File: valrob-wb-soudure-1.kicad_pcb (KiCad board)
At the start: 2 copper layers, 31 parts, among them J1 Conn_01x03, J2 Conn_01x06, J3 Conn_01x02, J4 Conn_01x02, J5 Conn_01x02, J6 Conn_01x02, Q1 2N7000, SW1 SW_Push, SW2 SW_Push, SW3 SW_Push, SW4 SW_Push

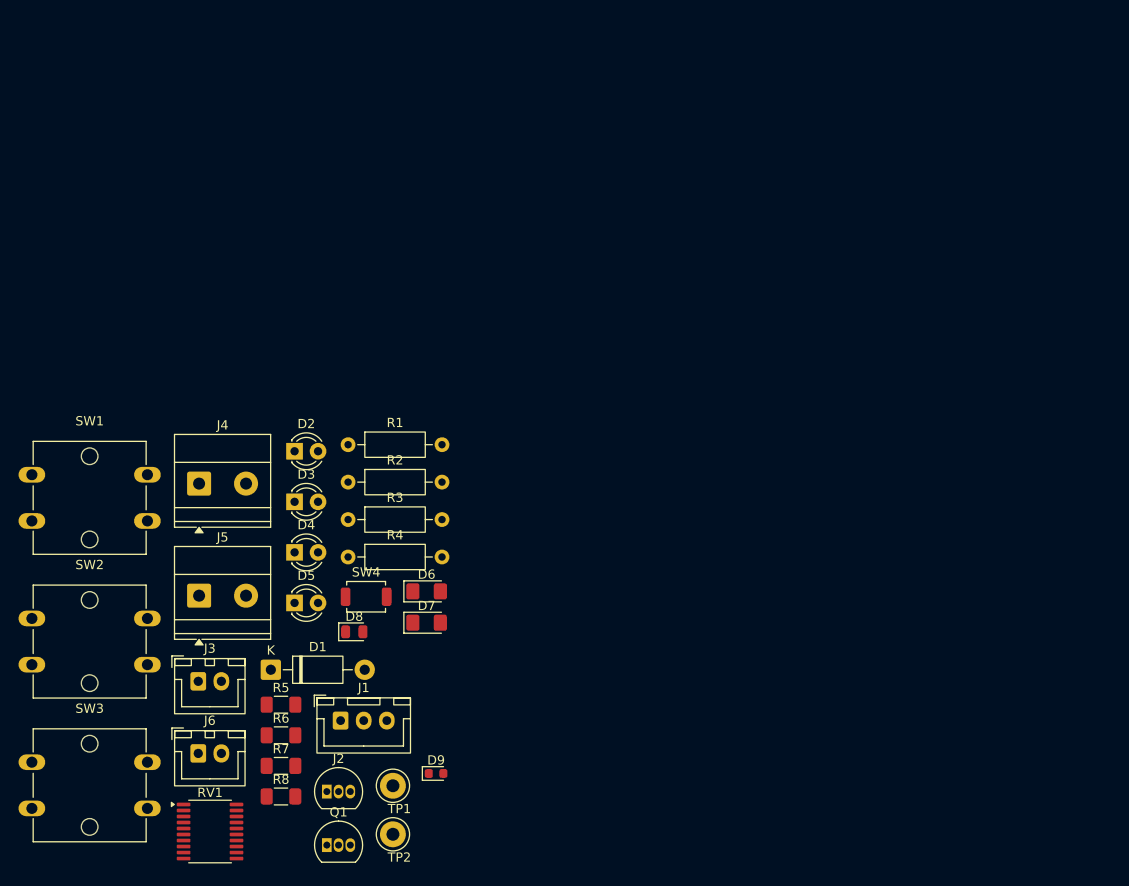
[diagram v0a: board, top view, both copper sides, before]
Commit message: pcb: initial sectionning
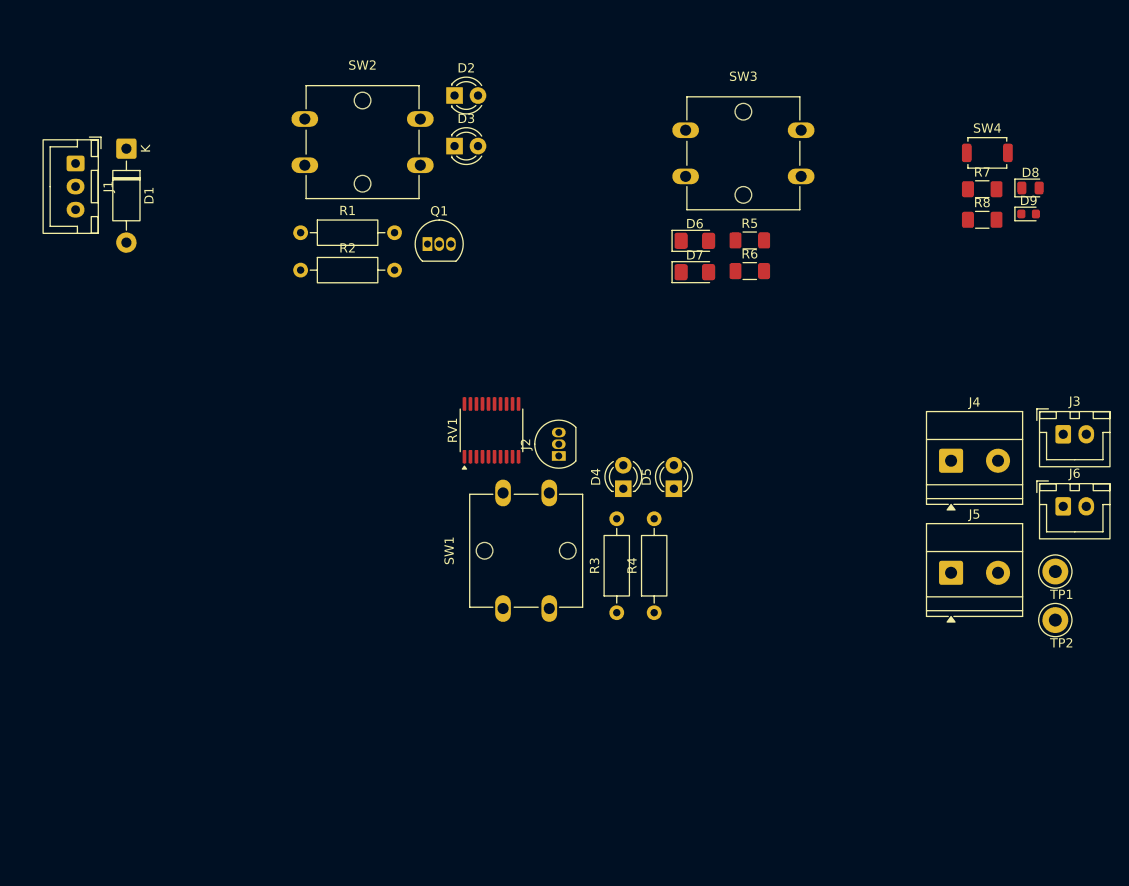
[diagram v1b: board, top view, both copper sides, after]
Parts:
- moved SW3 98.4 mm to (118.8, 103.2)
- moved R7 98.2 mm to (150.8, 109.6)
- moved R8 98.2 mm to (150.8, 112.9)
- moved J3 97.3 mm to (159.6, 136.2)
- moved J6 97.3 mm to (159.6, 143.9)
- moved D9 88.2 mm to (155.9, 112.3)
- moved D8 87.5 mm to (156.1, 109.5)
- moved SW4 82.6 mm to (151.4, 105.7)
- moved J4 81.4 mm to (147.5, 139.0)
- moved J5 81.4 mm to (147.5, 151.1)
- moved TP1 75.3 mm to (158.8, 151.0)
- moved TP2 75.3 mm to (158.8, 156.2)
- moved R6 71.4 mm to (125.7, 118.5)
- moved R5 71.4 mm to (125.7, 115.2)
- moved J1 66.7 mm to (52.8, 106.8), turned to -90 degrees
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
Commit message: pcb: add pot 3d model
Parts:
- RV1: footprint Package_SO:TSSOP-20_4.4x6.5mm_P0.65mm -> Potentiometer_THT:Potentiometer_Alps_RK09Y11_Single_Horizontal
- moved R2 25.5 mm to (87.0, 94.9), turned to -90 degrees
- moved D2 24.5 mm to (79.0, 119.0), turned to 90 degrees
- moved SW3 21.4 mm to (98.0, 98.0)
- moved D3 15.6 mm to (87.0, 119.0), turned to 90 degrees
- moved SW2 10.4 mm to (68.0, 98.0)
- moved R1 8.51 mm to (68.9, 112.0)
- moved D1 6.97 mm to (60.0, 112.0), turned to 90 degrees
- moved Q1 6.22 mm to (85.7, 112.0)
- moved RV1 5.90 mm to (95.0, 130.5), turned to 0 degrees
- moved J1 2.95 mm to (52.0, 104.0)

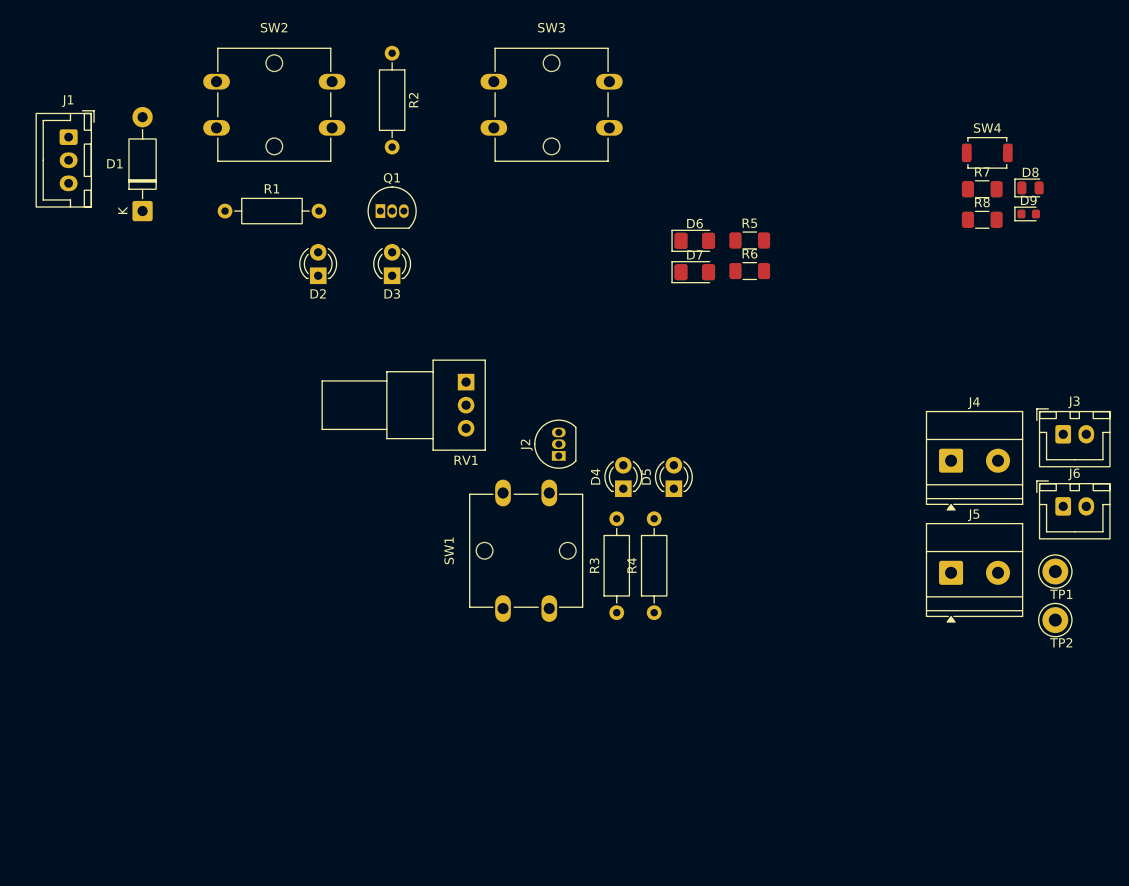
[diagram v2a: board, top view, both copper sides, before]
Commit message: pcb: initial layout
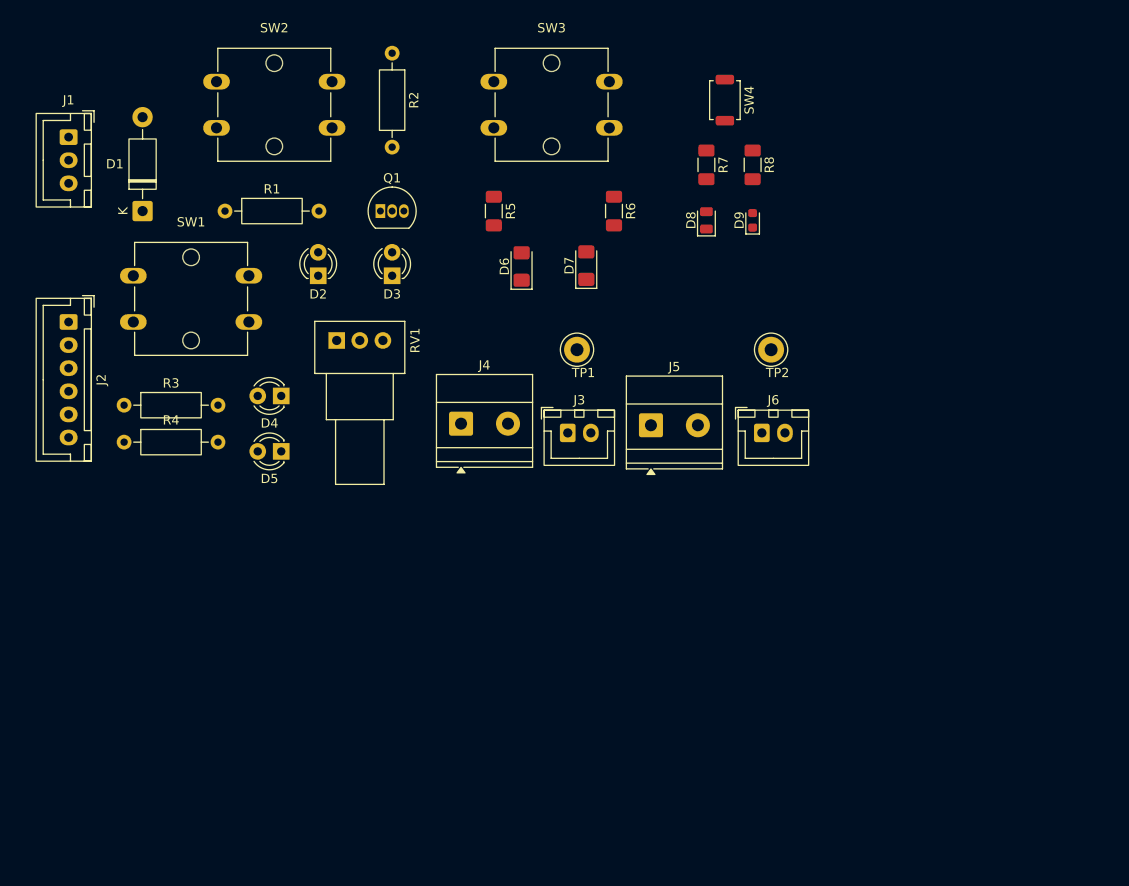
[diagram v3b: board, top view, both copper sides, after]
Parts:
- J2: footprint Package_TO_SOT_THT:TO-92_Inline -> Connector_JST:JST_XH_B6B-XH-A_1x06_P2.50mm_Vertical
- moved R4 60.2 mm to (58.0, 137.0), turned to 0 degrees
- moved R3 57.8 mm to (58.0, 133.0), turned to 0 degrees
- moved TP1 57.0 mm to (107.0, 127.0)
- moved J2 55.0 mm to (52.0, 124.0), turned to -90 degrees
- moved SW1 53.8 mm to (59.0, 119.0), turned to 0 degrees
- moved J3 53.6 mm to (106.0, 136.0)
- moved J4 53.2 mm to (94.5, 135.0)
- moved D5 42.7 mm to (75.0, 138.0), turned to 180 degrees
- moved TP2 42.4 mm to (128.0, 127.0)
- moved D4 38.3 mm to (75.0, 132.0), turned to 180 degrees
- moved J5 36.2 mm to (115.0, 135.2)
- moved D8 35.2 mm to (121.0, 113.0), turned to 90 degrees
- moved J6 33.6 mm to (127.0, 136.0)
- moved R7 30.0 mm to (121.0, 107.0), turned to -90 degrees
- moved D9 29.9 mm to (126.0, 113.0), turned to 90 degrees
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
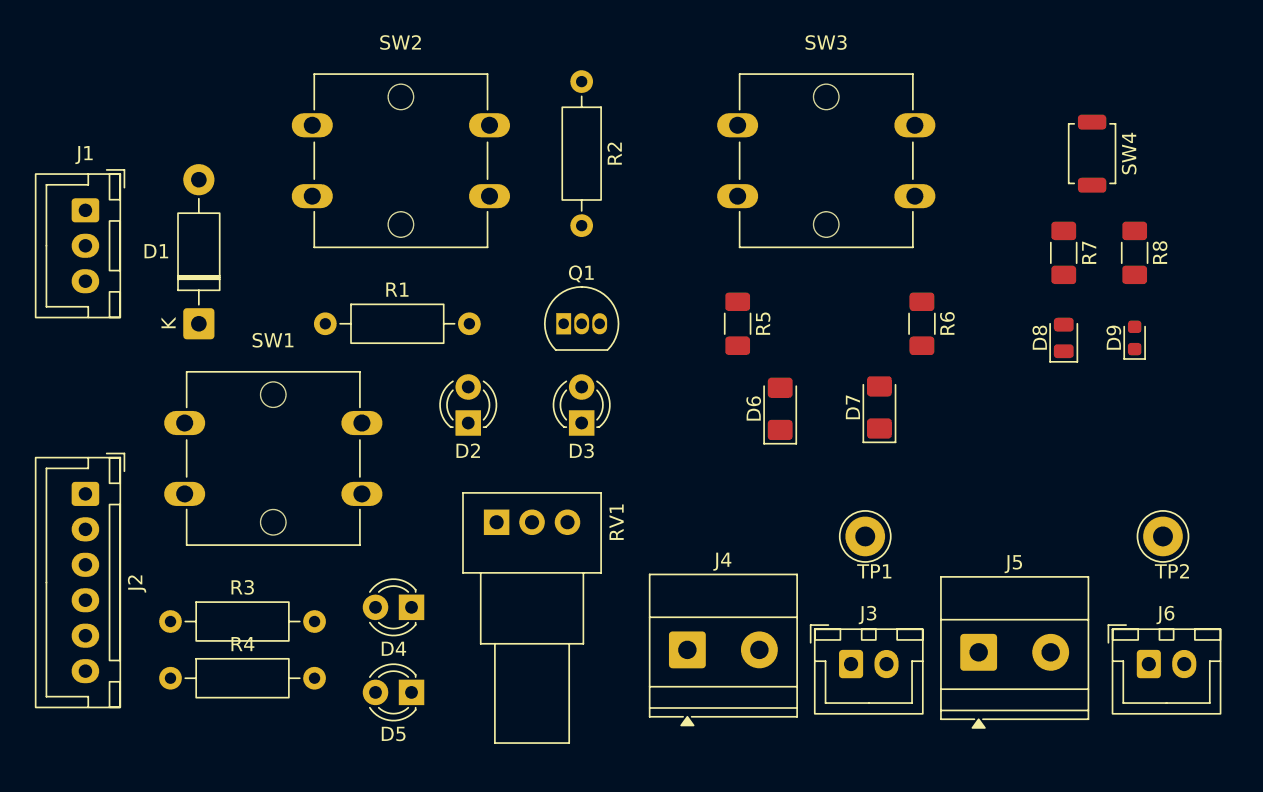
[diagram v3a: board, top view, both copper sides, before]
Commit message: pcb: add edge cut
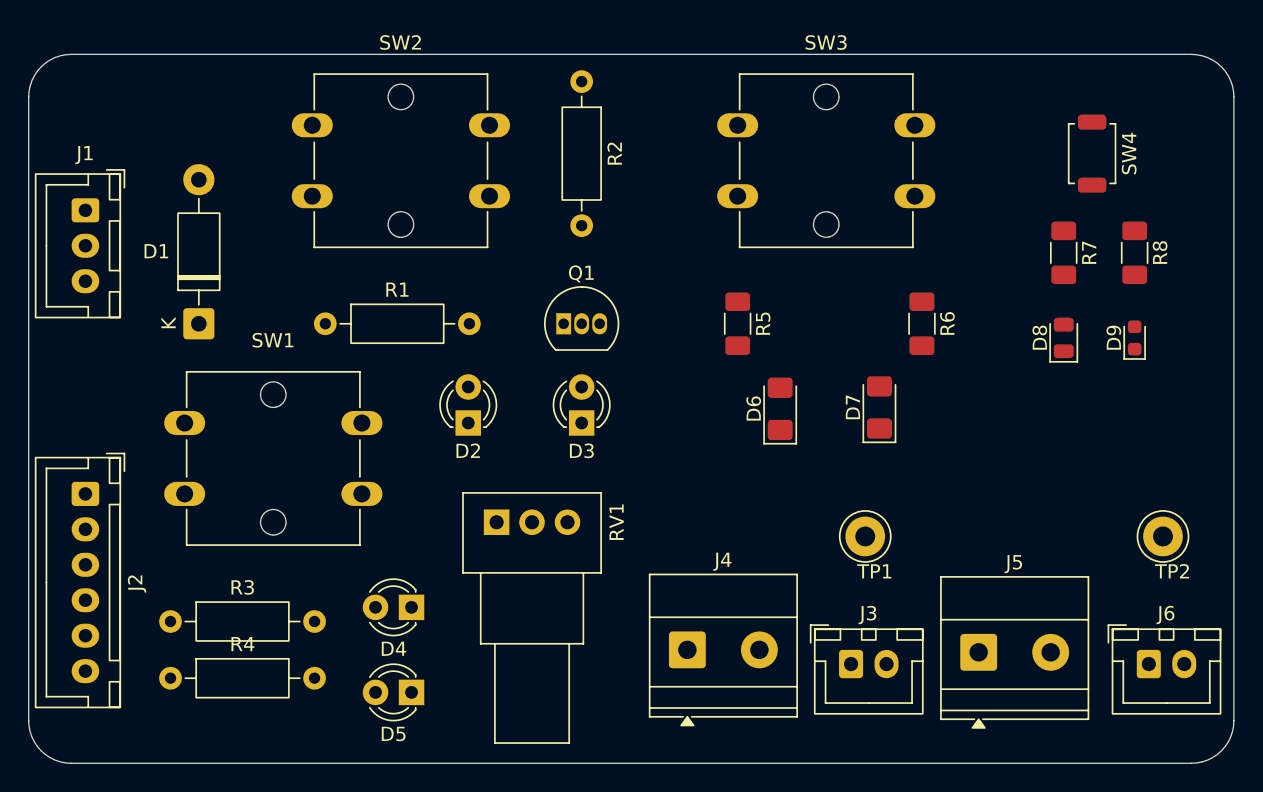
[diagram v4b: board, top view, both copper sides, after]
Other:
- board outline added: 85 x 50 mm
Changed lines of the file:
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@@
 		)
+	)
+	(gr_arc
+		(start 48 96)
+		(mid 48.87868 93.87868)
+		(end 51 93)
+		(stroke
+			(width 0.05)
+			(type default)
+		)
+		(layer "Edge.Cuts")
+	)
+	(gr_line
+		(start 48 140)
+		(end 48 96)
+		(stroke
+			(width 0.05)
+			(type default)
+		)
+		(layer "Edge.Cuts")
+	)
+	(gr_line
+		(start 51 93)
+		(end 130 93)
+		(stroke
+			(width 0.05)
+			(type default)
+		)
+		(layer "Edge.Cuts")
+	)
+	(gr_arc
+		(start 51 143)
+		(mid 48.87868 142.12132)
+		(end 48 140)
+		(stroke
+			(width 0.05)
+			(type default)
+		)
+		(layer "Edge.Cuts")
+	)
+	(gr_arc
+		(start 130 93)
+		(mid 132.12132 93.87868)
+		(end 133 96)
+		(stroke
+			(width 0.05)
+			(type default)
+		)
+		(layer "Edge.Cuts")
+	)
+	(gr_line
+		(start 130 143)
+		(end 51 143)
+		(stroke
+			(width 0.05)
+			(type default)
+		)
+		(layer "Edge.Cuts")
+	)
+	(gr_line
+		(start 133 96)
+		(end 133 140)
+		(stroke
+			(width 0.05)
+			(type default)
+		)
+		(layer "Edge.Cuts")
+	)
+	(gr_arc
+		(start 133 140)
+		(mid 132.12132 142.12132)
+		(end 130 143)
+		(stroke
+			(width 0.05)
+			(type default)
+		)
+		(layer "Edge.Cuts")
 	)
 	(embedded_fonts no)

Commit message: schem/pcb: add M3 mouting holes
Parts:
- added H1: MountingHole_Pad, MountingHole:MountingHole_3.2mm_M3_Pad_Via, F.Cu at (128.0, 98.0)
- added H2: MountingHole_Pad, MountingHole:MountingHole_3.2mm_M3_Pad_Via, F.Cu at (53.0, 98.0)
- added H3: MountingHole_Pad, MountingHole:MountingHole_3.2mm_M3_Pad_Via, F.Cu at (128.0, 138.0)
- added H4: MountingHole_Pad, MountingHole:MountingHole_3.2mm_M3_Pad_Via, F.Cu at (53.0, 138.0)
- moved J6 15.6 mm to (117.0, 124.0)
- moved J2 6.00 mm to (52.0, 118.0)
- moved D8 3.00 mm to (118.0, 113.0)
- moved D9 3.00 mm to (123.0, 113.0)
- moved R7 3.00 mm to (118.0, 107.0)
- moved R8 3.00 mm to (123.0, 107.0)
- moved SW4 3.00 mm to (120.0, 100.0)
- moved TP2 3.00 mm to (128.0, 124.0), turned to 180 degrees
- moved J1 2.00 mm to (52.0, 106.0)
